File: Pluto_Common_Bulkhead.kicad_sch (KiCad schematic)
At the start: 47 parts

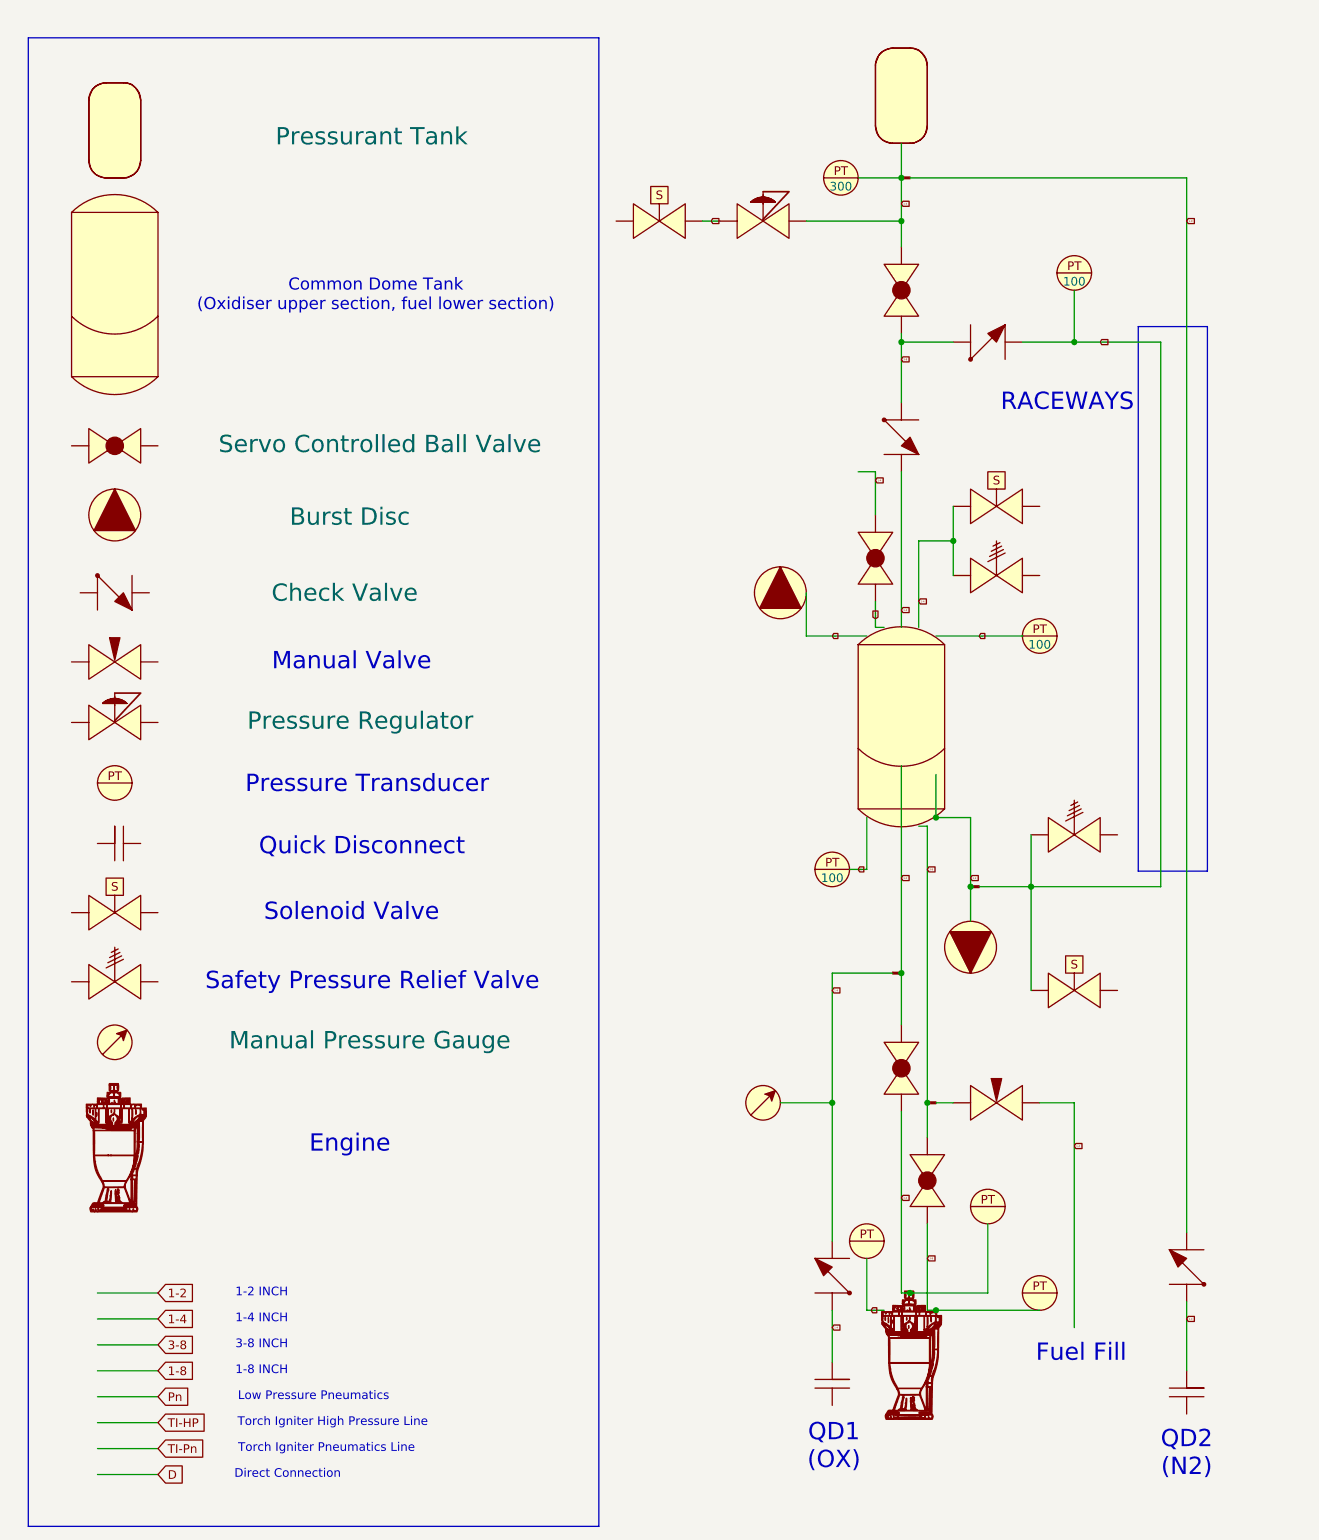
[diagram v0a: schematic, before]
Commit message: Updated Pluto pnid
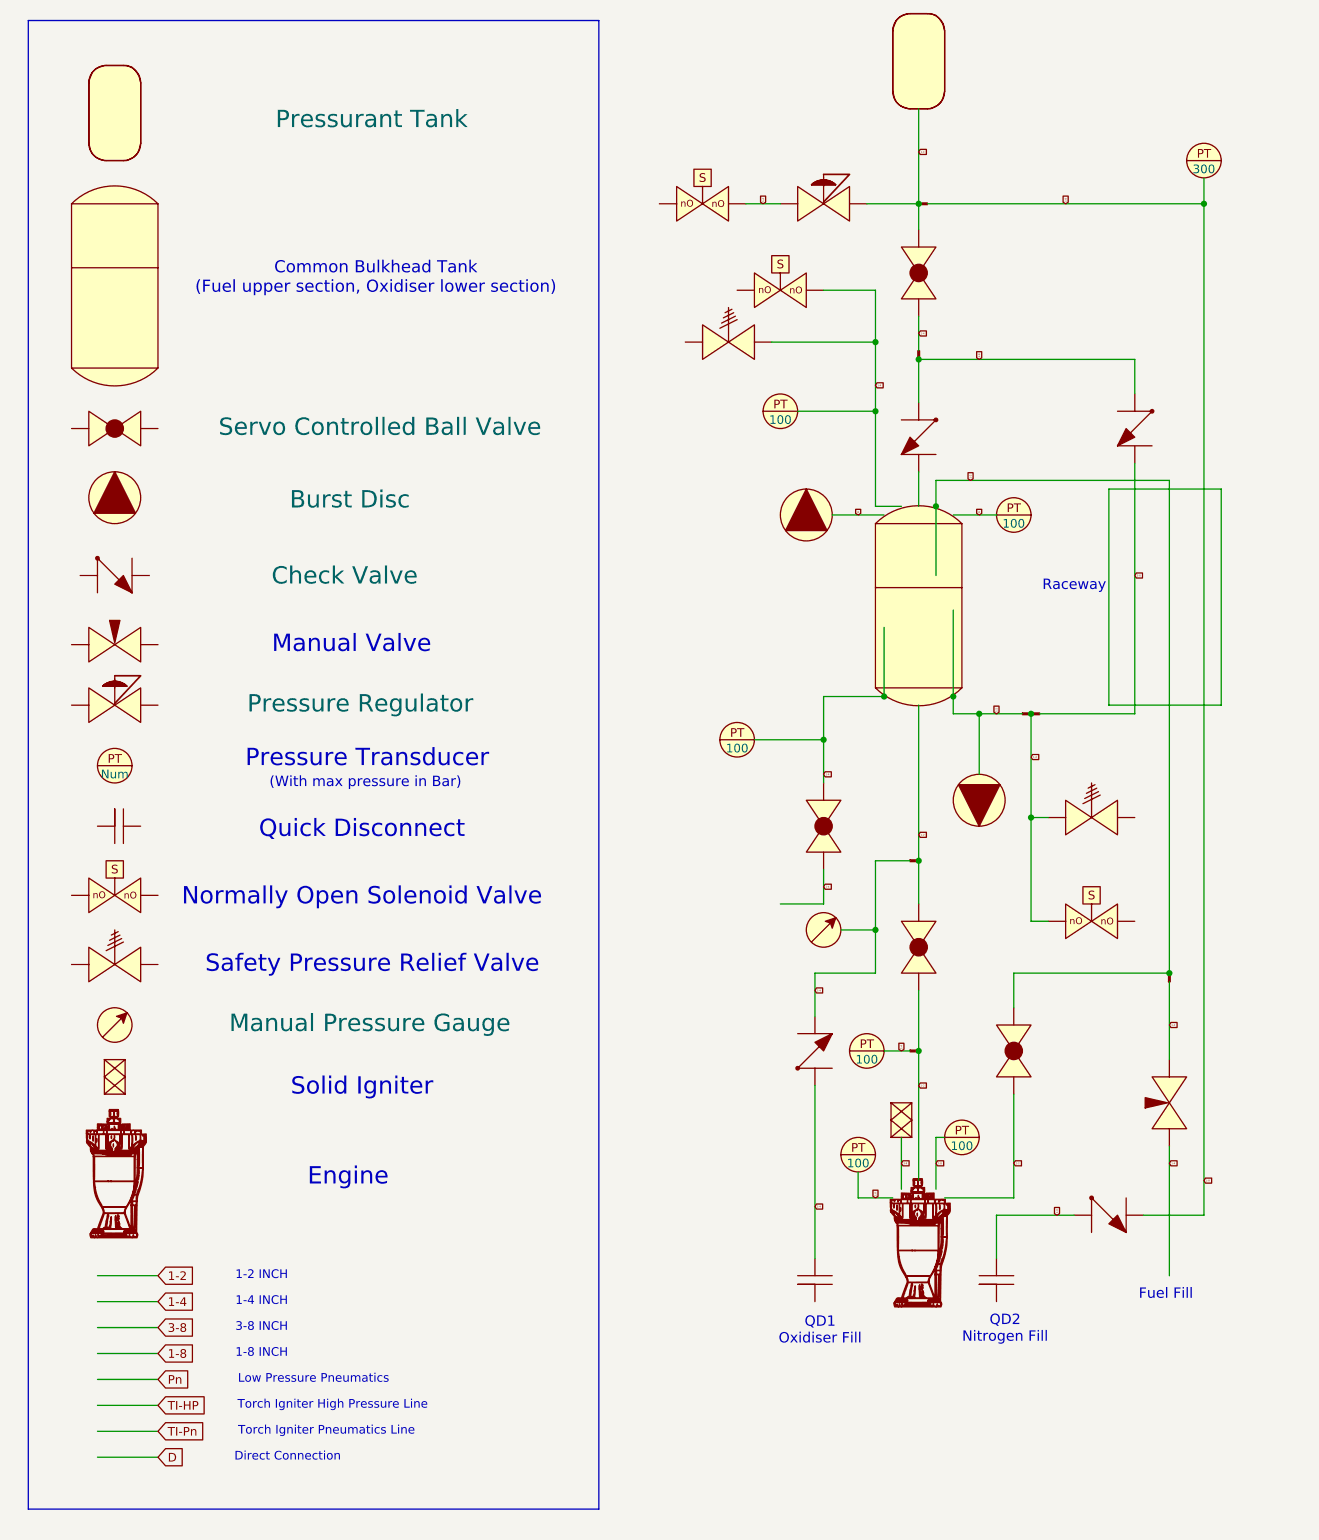
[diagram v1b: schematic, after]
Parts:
- removed BV11, Ball_Valve1, Ball_Valve2, Ball_Valve3: ~, symbol PID_symbols:Ball_Valve
- removed Ball_Valve(ServoControlled)100: Servo Controlled Ball Valve, symbol PID_symbols:Ball_Valve
- removed BurstDisc123: Burst Disc, symbol PID_symbols:Burst_Disc
- removed Burst_Disc4, Burst_Disc7: ~, symbol PID_symbols:Burst_Disc
- removed Check_Valve112: Check Valve, symbol PID_symbols:Check_Valve
- removed Check_Valve2, Check_Valve3, Check_Valve4, Check_Valve5: ~, symbol PID_symbols:Check_Valve
- removed CommonDomeTank1, CommonDomeTank2: ~, symbol PID_symbols:Common_Dome_Tank
- removed Engine2, Engine3: ~, symbol PID_symbols:Engine
- removed Manual_Pressure_Gauge2: ~, symbol PID_symbols:Manual_Pressure_Gauge
- removed Manual_Pressure_Gauge3: Manual Pressure Gauge, symbol PID_symbols:Manual_Pressure_Gauge
- removed Needle_Valve2, Needle_Valve3: ~, symbol PID_symbols:Needle_Valve
- removed NitrogenTank1: ~, symbol PID_symbols:Tank
- removed PT10, PT14, PT9: 100, symbol PID_symbols:Pressure_Transducer
- removed PT11: 300, symbol PID_symbols:Pressure_Transducer
- removed PT15, PT37, PT38, PT7: ~, symbol PID_symbols:Pressure_Transducer
- removed Pressure_Regulator123: Pressure Regulator, symbol PID_symbols:Pressure_Regulator
- removed QD6, QD7, QD8: ~, symbol PID_symbols:Quick_Disconnect
- removed Reg8: ~, symbol PID_symbols:Pressure_Regulator
- removed SPRV3, SPRV4, SPRV5: ~, symbol PID_symbols:SPRV
- removed Solenoid1, Solenoid2, Solenoid3, Solenoid4: ~, symbol PID_symbols:Solenoid
- removed Tank200: Pressurant Tank, symbol PID_symbols:Tank
- removed U2, U3, U4, U5: ~, symbol PID_symbols:stop
- added BV30, BV31, BV32, BV33: ~, symbol PID_symbols:Ball_Valve
- added Ball_Valve(ServoControlled)102: Servo Controlled Ball Valve, symbol PID_symbols:Ball_Valve
- added BurstDisc125: Burst Disc, symbol PID_symbols:Burst_Disc
- added Burst_Disc12, Burst_Disc13: ~, symbol PID_symbols:Burst_Disc
- added CV32, CV33, CV34, CV6: ~, symbol PID_symbols:Check_Valve
- added Check_Valve114: Check Valve, symbol PID_symbols:Check_Valve
- added Engine10, Engine9: ~, symbol PID_symbols:Engine
- added Manual_Pressure_Gauge5: Manual Pressure Gauge, symbol PID_symbols:Manual_Pressure_Gauge
- added Manual_Pressure_Gauge6: ~, symbol PID_symbols:Manual_Pressure_Gauge
- added Needle_Valve7, Needle_Valve8: ~, symbol PID_symbols:Needle_Valve
- added PT56: Num, symbol PID_symbols:Pressure_Transducer
- added PT57, PT59, PT60, PT61, PT62, PT63: 100, symbol PID_symbols:Pressure_Transducer
- added PT58: 300, symbol PID_symbols:Pressure_Transducer
- added Pressure_Regulator125: Pressure Regulator, symbol PID_symbols:Pressure_Regulator
- added QD16, QD17, QD18: ~, symbol PID_symbols:Quick_Disconnect
- added Reg13: ~, symbol PID_symbols:Pressure_Regulator
- added SPRV14, SPRV15, SPRV16: ~, symbol PID_symbols:SPRV
- added T13: ~, symbol PID_symbols:Tank
- added Tank202: Pressurant Tank, symbol PID_symbols:Tank
- added U24, U25: ~, symbol PID_symbols:Common_Bulkhead_Tank_F/0
- added U26, U28: ~, symbol PID_symbols:Solid_Igniter
- added U27, U29, U30, U31, U32, U33, U34: ~, symbol PID_symbols:stop
- added nO_Sol20, nO_Sol21, nO_Sol22, nO_Sol23: ~, symbol PID_symbols:Normally Open Solenoid
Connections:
- net 1-2: now also BV31., BV32., Burst_Disc13., Engine10., U25., U31., U32., U33., U34.
- net 1-4: now also BV30., BV33., CV32., CV34., Manual_Pressure_Gauge6., Needle_Valve8., PT59., PT62., PT63., QD17., QD18., Reg13., SPRV15., SPRV16., T13., U25., U27., U29., U30., U31., U32., U33., U34., nO_Sol20., nO_Sol21., nO_Sol22.
- net 1-8: now also CV34., Engine10., PT58., PT60., PT61., U27.
- net 3-8: now also CV33., CV6., Engine10., U28., U29., U30.
- net D: now also Burst_Disc12., PT57., U25.
- new net: CV6., U25.
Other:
- note added: "(With max pressure in Bar)"
- note added: "Common Bulkhead Tank (Fuel upper section, Oxidiser lower section)"
- note added: "Normally Open Solenoid Valve"
- note added: "QD1 Oxidiser Fill"
- note added: "QD2 Nitrogen Fill"
- note added: "Raceway"
- note added: "Solid Igniter"
- note removed: "Common Dome Tank (Oxidiser upper section, fuel lower section)"
- note removed: "QD1 (OX)"
- note removed: "QD2 (N2)"
- note removed: "RACEWAYS"
- note removed: "Solenoid Valve"
- company: ICLR -> (none)
- title: Pluto Propulsion P&ID -> (none)

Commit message: overwriting babz
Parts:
- renumbered BV30 to BV34, BV33 to BV35, BV32 to BV36, BV31 to BV37, Ball_Valve(ServoControlled)102 to Ball_Valve(ServoControlled)3, BurstDisc125 to BurstDisc3, Burst_Disc12 to Burst_Disc14, Burst_Disc13 to Burst_Disc15, CV33 to CV34, CV6 to CV35, CV32 to CV36, CV34 to CV37, Check_Valve114 to Check_Valve11, Engine9 to Engine11, Engine10 to Engine12, Manual_Pressure_Gauge6 to Manual_Pressure_Gauge5, Manual_Pressure_Gauge5 to Manual_Pressure_Gauge6, Needle_Valve8 to Needle_Valve10, Needle_Valve7 to Needle_Valve9, PT58 to PT59, PT59 to PT60, PT57 to PT61, PT63 to PT62, PT56 to PT63, PT62 to PT64, PT60 to PT65, PT61 to PT66, Pressure_Regulator125 to Pressure_Regulator3, QD16 to QD21, QD17 to QD22, QD18 to QD23, Reg13 to Reg15, SPRV15 to SPRV19, SPRV16 to SPRV20, SPRV14 to SPRV21, Tank202 to Tank3, U27 to U24, U24 to U25, U29 to U26, U25 to U27, U31 to U28, U30 to U29, U34 to U30, U32 to U31, U33 to U32, U26 to U33, U28 to U34, nO_Sol23 to nO_Sol22, nO_Sol22 to nO_Sol23
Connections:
- new net: CV35., U27.

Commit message: New year update
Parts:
- renumbered BV35 to BV53, BV34 to BV54, BV36 to BV55, BV37 to BV56, Ball_Valve(ServoControlled)3 to Ball_Valve(ServoControlled)5, BurstDisc3 to BurstDisc5, Burst_Disc14 to Burst_Disc24, Burst_Disc15 to Burst_Disc25, CV36 to CV55, CV35 to CV56, CV37 to CV57, CV34 to CV58, Check_Valve11 to Check_Valve17, Engine11 to Engine18, Engine12 to Engine19, Manual_Pressure_Gauge6 to Manual_Pressure_Gauge11, Manual_Pressure_Gauge5 to Manual_Pressure_Gauge12, Needle_Valve9 to Needle_Valve17, Needle_Valve10 to Needle_Valve18, PT61 to PT100, PT59 to PT101, PT63 to PT94, PT62 to PT95, PT60 to PT96, PT66 to PT97, PT64 to PT98, PT65 to PT99, Pressure_Regulator3 to Pressure_Regulator5, QD21 to QD38, QD22 to QD39, QD23 to QD40, Reg15 to Reg23, SPRV21 to SPRV32, SPRV19 to SPRV33, SPRV20 to SPRV34, T13 to T17, Tank3 to Tank5, U25 to U53, U33 to U54, U34 to U55, U26 to U56, U27 to U57, U30 to U58, U32 to U59, U24 to U60, U28 to U61, U29 to U62, U31 to U63, nO_Sol22 to nO_Sol34, nO_Sol20 to nO_Sol35, nO_Sol21 to nO_Sol36, nO_Sol23 to nO_Sol37
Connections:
- new net: CV56., U57.

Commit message: j0
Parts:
- renumbered BV54 to BV22, BV53 to BV23, BV55 to BV24, BV56 to BV25, Ball_Valve(ServoControlled)5 to Ball_Valve(ServoControlled)1, BurstDisc5 to BurstDisc1, Burst_Disc24 to Burst_Disc10, Burst_Disc25 to Burst_Disc11, CV58 to CV34, CV56 to CV35, CV55 to CV36, CV57 to CV37, Check_Valve17 to Check_Valve1, Engine18 to Engine5, Engine19 to Engine6, Manual_Pressure_Gauge12 to Manual_Pressure_Gauge6, Manual_Pressure_Gauge11 to Manual_Pressure_Gauge7, Needle_Valve17 to Needle_Valve7, Needle_Valve18 to Needle_Valve8, PT101 to PT32, PT96 to PT33, PT100 to PT34, PT95 to PT35, PT94 to PT36, PT98 to PT37, PT99 to PT38, PT97 to PT39, Pressure_Regulator5 to Pressure_Regulator1, QD40 to QD10, QD38 to QD8, QD39 to QD9, Reg23 to Reg9, SPRV33 to SPRV14, SPRV34 to SPRV15, SPRV32 to SPRV16, T17 to T9, Tank5 to Tank1, U60 to U25, U53 to U26, U56 to U27, U57 to U28, U61 to U29, U62 to U30, U58 to U31, U63 to U32, U59 to U33, U54 to U34, U55 to U35, nO_Sol35 to nO_Sol6, nO_Sol36 to nO_Sol7, nO_Sol34 to nO_Sol8, nO_Sol37 to nO_Sol9
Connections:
- new net: CV35., U28.

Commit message: more silwood stuff
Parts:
- renumbered Ball_Valve(ServoControlled)1 to BV1, BV23 to BV21, BV24 to BV23, BV25 to BV24, BurstDisc1 to Burst_Disc1, Check_Valve1 to CV1, CV36 to CV34, CV37 to CV36, CV34 to CV37, Engine5 to Engine6, Engine6 to Engine7, Manual_Pressure_Gauge7 to Manual_Pressure_Gauge8, Manual_Pressure_Gauge6 to Manual_Pressure_Gauge9, PT36 to PT45, PT35 to PT46, PT33 to PT47, PT39 to PT48, PT37 to PT49, PT38 to PT50, PT34 to PT51, PT32 to PT52, QD9 to QD10, QD10 to QD11, QD8 to QD9, SPRV14 to SPRV17, SPRV15 to SPRV18, Pressure_Regulator1 to Servo_Reg1, Reg9 to Servo_Reg9, Tank1 to T1, U26 to U40, U34 to U41, U35 to U42, U27 to U43, U28 to U44, U31 to U45, U33 to U46, U25 to U47, U29 to U48, U30 to U49, U32 to U50, nO_Sol7 to nO_Sol10, nO_Sol9 to nO_Sol11, nO_Sol6 to nO_Sol9
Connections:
- new net: CV35., U44.

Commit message: Formatiing
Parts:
- renumbered BV21 to BV53, BV22 to BV54, BV23 to BV55, BV24 to BV56, BV1 to Ball_Valve(ServoControlled)5, Burst_Disc1 to BurstDisc5, Burst_Disc10 to Burst_Disc24, Burst_Disc11 to Burst_Disc25, CV34 to CV55, CV35 to CV56, CV36 to CV57, CV37 to CV58, CV1 to Check_Valve17, Engine6 to Engine18, Engine7 to Engine19, Manual_Pressure_Gauge8 to Manual_Pressure_Gauge11, Manual_Pressure_Gauge9 to Manual_Pressure_Gauge12, Needle_Valve7 to Needle_Valve17, Needle_Valve8 to Needle_Valve18, PT51 to PT100, PT52 to PT101, PT45 to PT94, PT46 to PT95, PT47 to PT96, PT48 to PT97, PT49 to PT98, PT50 to PT99, Servo_Reg1 to Pressure_Regulator5, QD9 to QD38, QD10 to QD39, QD11 to QD40, Servo_Reg9 to Reg23, SPRV16 to SPRV32, SPRV17 to SPRV33, SPRV18 to SPRV34, T9 to T17, T1 to Tank5, U40 to U53, U41 to U54, U42 to U55, U43 to U56, U44 to U57, U45 to U58, U46 to U59, U47 to U60, U48 to U61, U49 to U62, U50 to U63, nO_Sol8 to nO_Sol34, nO_Sol9 to nO_Sol35, nO_Sol10 to nO_Sol36, nO_Sol11 to nO_Sol37
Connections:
- new net: CV56., U57.
